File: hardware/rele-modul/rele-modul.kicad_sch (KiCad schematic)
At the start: 36 parts, among them J100 24V IN, J101 RELÉ 1, J102 RELÉ 2, J103 RELÉ 3, J104 RELÉ 4, J105 SCT-013, K1 RTD14024, K2 RTD14024, K3 RTD14024, K4 RTD14024, U101 ULN2803ADWR

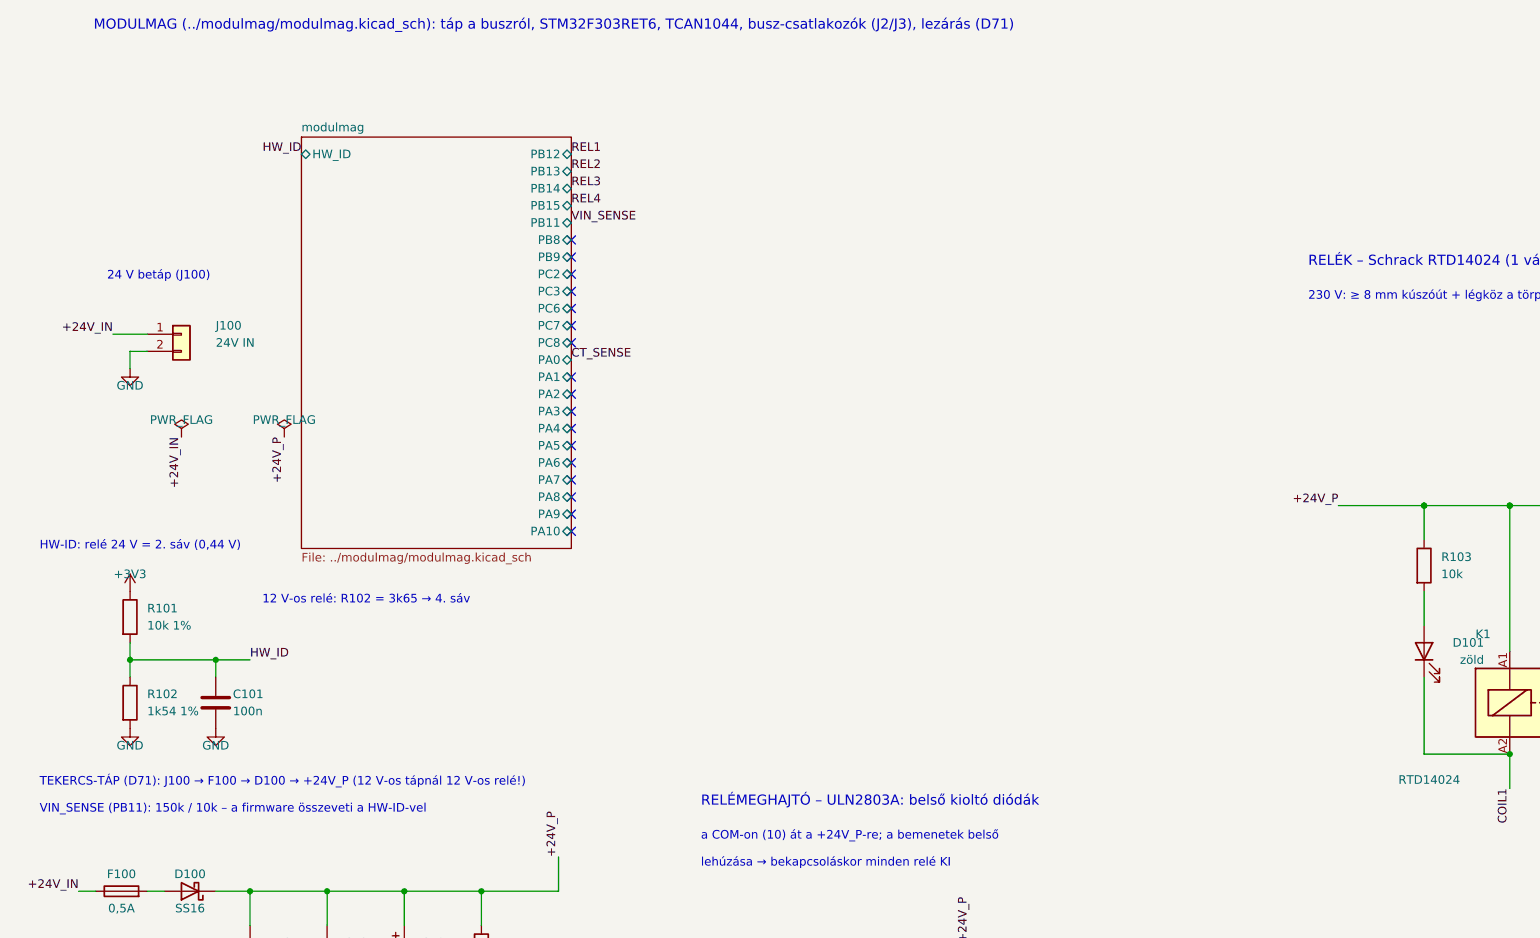
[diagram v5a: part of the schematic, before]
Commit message: Hardver: szakértői javítások (D74–D77), STM32L433 + SN65HVD230 + GND-ági polaritásvédelem (D78–D81), teljes ellenőrzés
- D74–D77: busz-GND ellenállás, CAN-fojtó-hely, TVS a +5V_BUCK-on és a VUSB-n, bemenetvédelem,
  230 V-os és antenna-tiltás a NYÁK-on, SCT-jack footprint
- D78–D80: modul-MCU STM32L433RCT3 (VIN_SENSE PB1, LED: TIM15/TIM16, I_SENSE PA3), modul-transceiver
  SN65HVD230, N-FET a GND-ágban (vezérlő Q1, LED Q201, relé Q100), MCP9701A, táp-LED a +5V-ról,
  2 oz a LED-/relémodulon, AP2112K marad; D81 javaslat (TPD4E02B04 a bemeneteken)
- CubeMX-projektek L433-ra, fejsoros kódgenerálással ellenőrizve (minden periféria inicializálódik)
- gen/ellenorzes.py (ERC, láb ↔ pad, modulmag, CubeMX, polaritásvédelem, NYÁK ↔ rajz, DRC) – 0 hiba
- gen/bom.sh + bom/*.csv darabjegyzék; docs/komponenslista.md a konzulensnek
- kontextus: DONTESEK D74–D81, specifikációk, ATTEKINTES, NAPLO, beszerzési lista; alkatrészkészlet-jegyzet (claude.ai)

Co-Authored-By: Claude Opus 5.5 <noreply@anthropic.com>
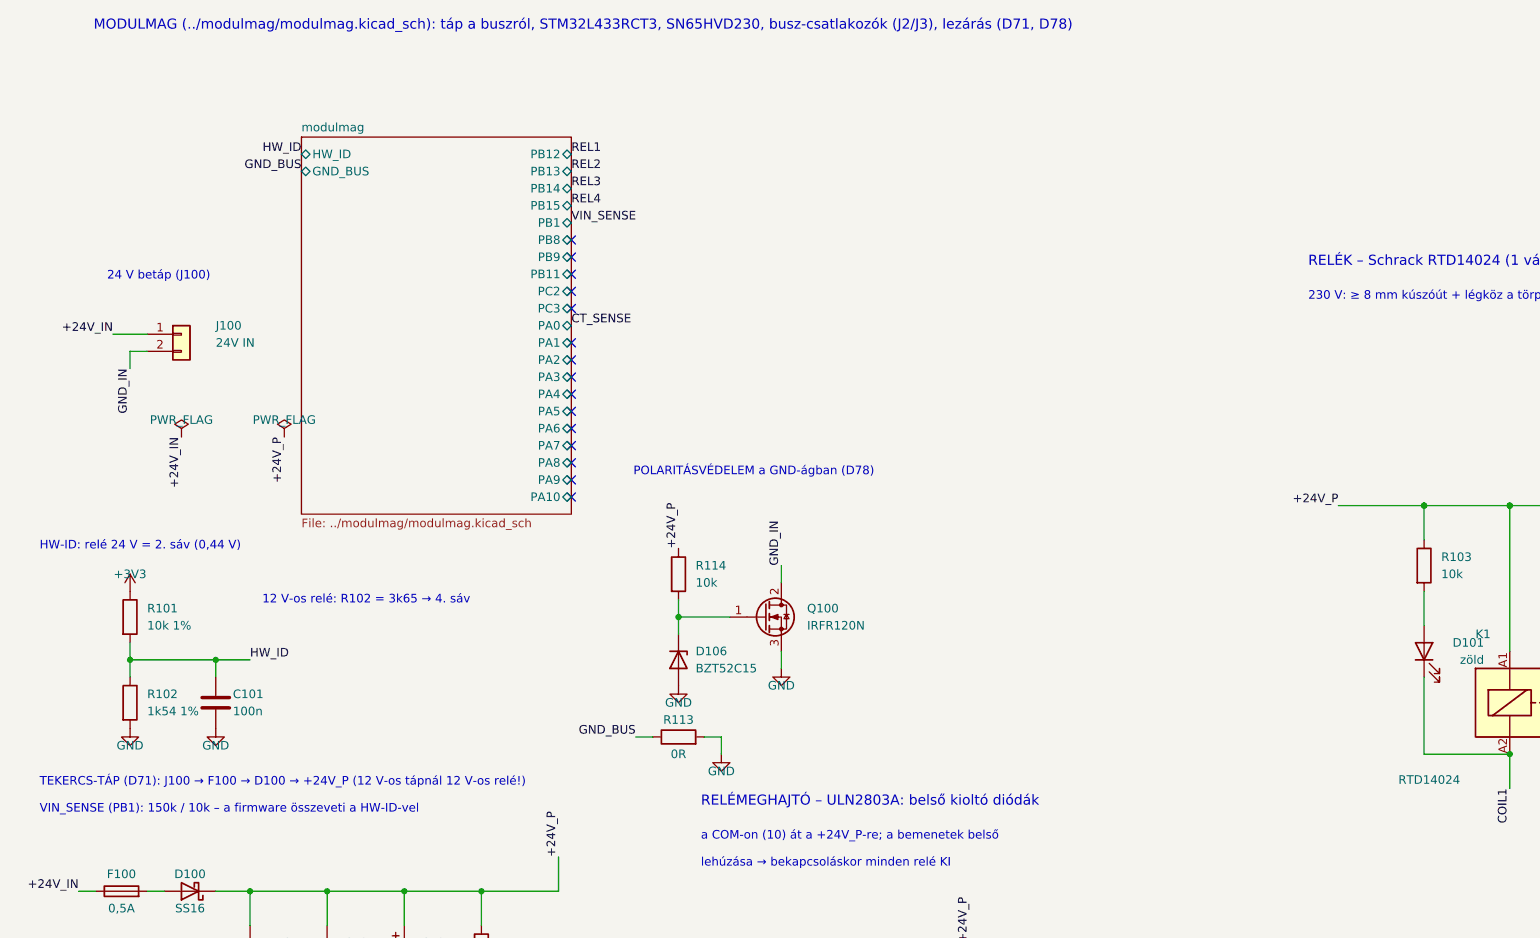
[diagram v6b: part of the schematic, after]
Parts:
- added D106: BZT52C15, Diode_SMD:D_SOD-123, symbol Device:D_Zener
- added Q100: IRFR120N, Package_TO_SOT_SMD:TO-252-2, symbol Transistor_FET:Q_NMOS_GDS
- added R113: 0R, Resistor_SMD:R_1206_3216Metric, symbol Device:R
- added R114: 10k, Resistor_SMD:R_0603_1608Metric, symbol Device:R
- J101, J102, J103, J104: Megjegyzés 1 = COM, 2 = NO; ≥ 16 A, ≥ 250 V AC; helyőrző – push-in, a 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 -> 1 = COM, 2 = NO; ≥ 16 A, ≥ 250 V AC; push-in (D79) – a típu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
- J105: footprint Connector_Audio:Jack_3.5mm_CUI_SJ1-3523N_Horizontal -> Connector_Audio:Jack_3.5mm_CUI_SJ1-3513N_Horizontal
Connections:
- net +24V_P: now also R114.1
- net GND: now also D106.2 (A), Q100.3 (S), R113.2; no longer J100.2 (Pin_2)
- new net: D106.1 (K), Q100.1 (G), R114.2
- new net GND_BUS: R113.1
- new net GND_IN: J100.2 (Pin_2), Q100.2 (D)
- no-connect marks 26 -> 24
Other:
- sheet modulmag ports: added GND_BUS, PB1; removed PC6, PC7, PC8
- note added: "MODULMAG (../modulmag/modulmag.kicad_sch): táp a buszról, STM32L433RCT3, SN65HVD230, busz-csatlakozók (J2/J3), lezárás (D71, D78)"
- note added: "POLARITÁSVÉDELEM a GND-ágban (D78)"
- note added: "VIN_SENSE (PB1): 150k / 10k – a firmware összeveti a HW-ID-vel"
- note removed: "MODULMAG (../modulmag/modulmag.kicad_sch): táp a buszról, STM32F303RET6, TCAN1044, busz-csatlakozók (J2/J3), lezárás (D71)"
- note removed: "VIN_SENSE (PB11): 150k / 10k – a firmware összeveti a HW-ID-vel"

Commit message: Hardver: relékimenet 5,08 mm-es THT sorkapocs (D83), D81 elvetve – marad a TPD4E05U06
Co-Authored-By: Claude Opus 5.5 <noreply@anthropic.com>
Claude-Session: https://claude.ai/code/session_01KVtZMUPbtveTXy9VyJshyt
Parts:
- J101, J102, J103, J104: Megjegyzés 1 = COM, 2 = NO; ≥ 16 A, ≥ 250 V AC; push-in (D79) – a típu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 -> 1 = COM, 2 = NO; 5,08 mm-es THT sorkapocs a készletből (D83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
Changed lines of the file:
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@@
 			)
 		)
-		(property "Megjegyzés" "1 = COM, 2 = NO; ≥ 16 A, ≥ 250 V AC; push-in (D79) – a típus és a footprint a DIN-ház vállától függ, ez helyőrző"
+		(property "Megjegyzés" "1 = COM, 2 = NO; 5,08 mm-es THT sorkapocs a készletből (D83) – névleges érték ≥ 16 A, ≥ 250 V AC"
 			(at 360.68 124.46 0)
 			(hide yes)
@@
 			)
 		)
-		(property "Megjegyzés" "1 = COM, 2 = NO; ≥ 16 A, ≥ 250 V AC; push-in (D79) – a típus és a footprint a DIN-ház vállától függ, ez helyőrző"
+		(property "Megjegyzés" "1 = COM, 2 = NO; 5,08 mm-es THT sorkapocs a készletből (D83) – névleges érték ≥ 16 A, ≥ 250 V AC"
 			(at 260.35 214.63 0)
 			(hide yes)
@@
 			)
 		)
-		(property "Megjegyzés" "1 = COM, 2 = NO; ≥ 16 A, ≥ 250 V AC; push-in (D79) – a típus és a footprint a DIN-ház vállától függ, ez helyőrző"
+		(property "Megjegyzés" "1 = COM, 2 = NO; 5,08 mm-es THT sorkapocs a készletből (D83) – névleges érték ≥ 16 A, ≥ 250 V AC"
 			(at 360.68 214.63 0)
 			(hide yes)
@@
 			)
 		)
-		(property "Megjegyzés" "1 = COM, 2 = NO; ≥ 16 A, ≥ 250 V AC; push-in (D79) – a típus és a footprint a DIN-ház vállától függ, ez helyőrző"
+		(property "Megjegyzés" "1 = COM, 2 = NO; 5,08 mm-es THT sorkapocs a készletből (D83) – névleges érték ≥ 16 A, ≥ 250 V AC"
 			(at 260.35 124.46 0)
 			(hide yes)
